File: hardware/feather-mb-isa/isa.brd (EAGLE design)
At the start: 91.4 x 95.2 mm, 16 parts, among them J1 EDGE-80PTH-RA, J2 M22PTH, J3 GREEN-3P-5.0, J4 GREEN-3P-5.0, J5 GREEN-3P-5.0, J6 GREEN-3P-5.0

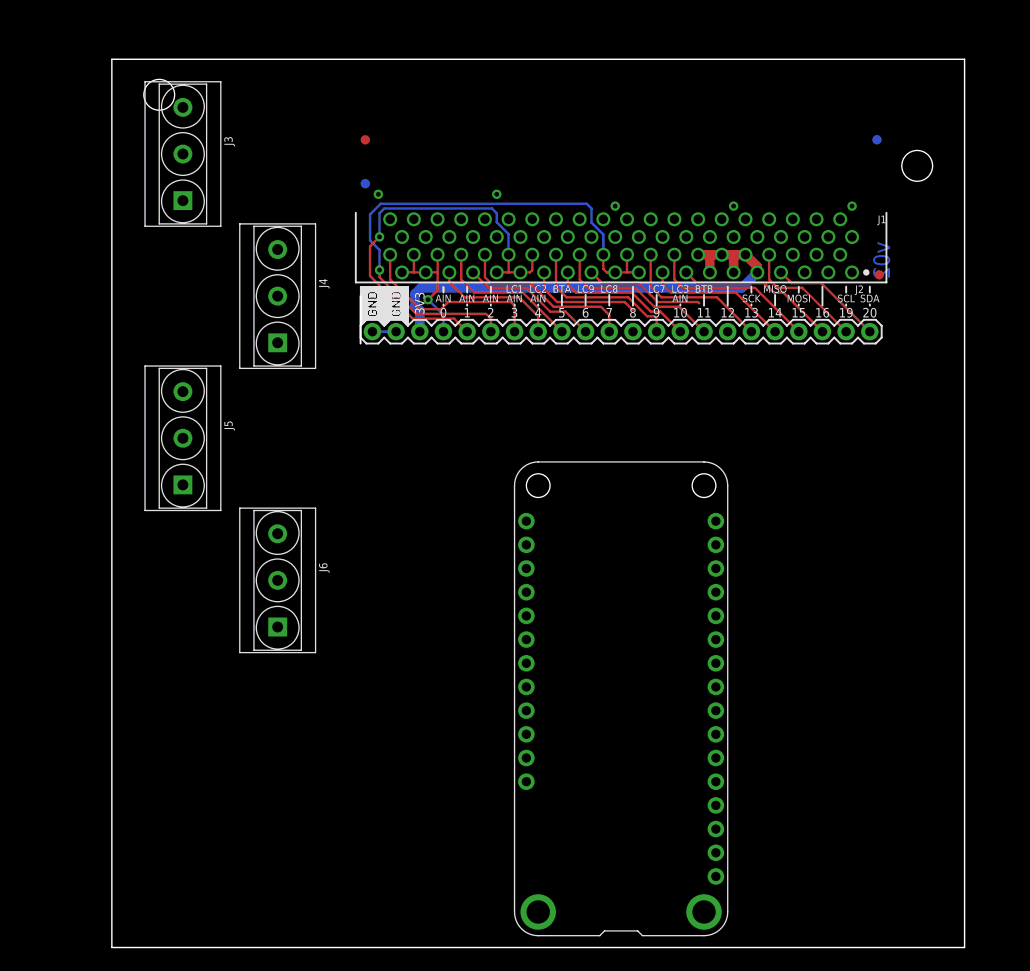
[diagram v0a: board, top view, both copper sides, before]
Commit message: Renamed midi.py
Now can be main.

Updated hardware. Looks ready for layout. Need to do some more
work in the middle. What to do with that space? Some neopixels?

Some buttons?

More headers?
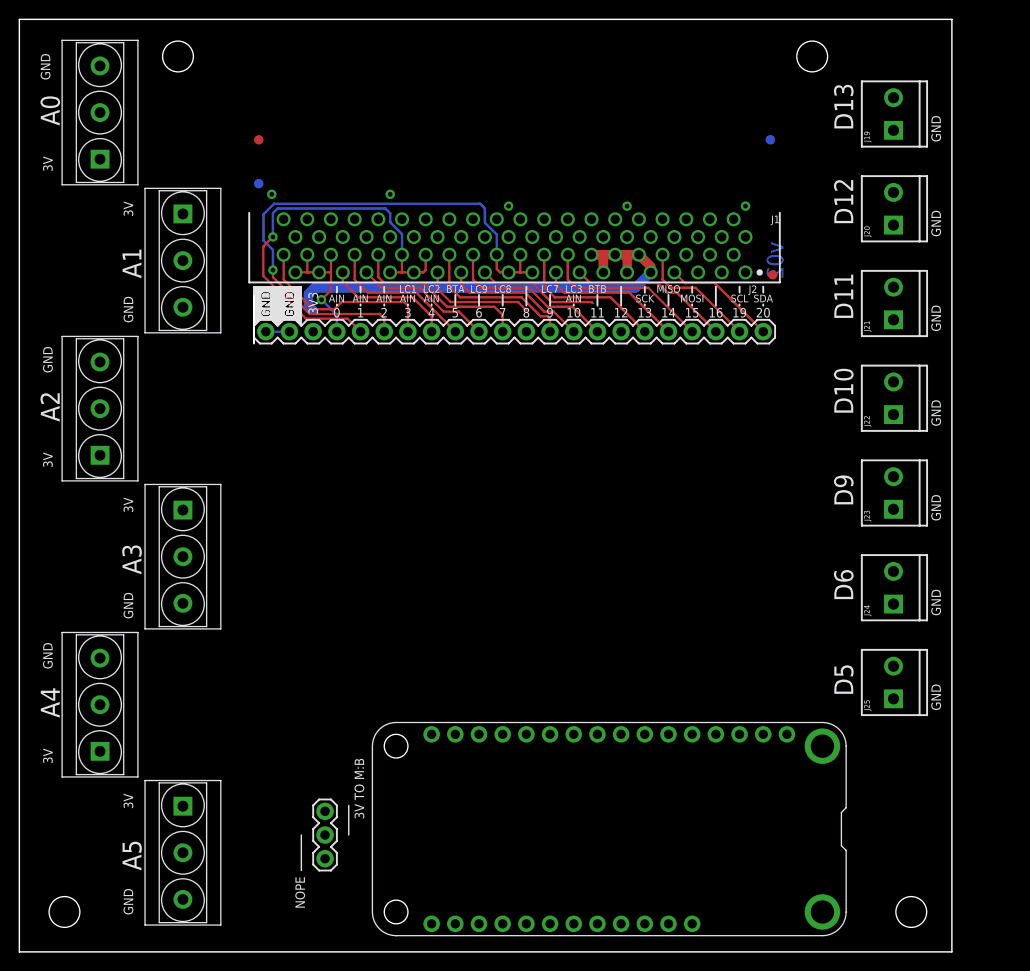
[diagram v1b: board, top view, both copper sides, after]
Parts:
- added H3, H4: STAND-OFF, SparkFun-Electromechanical:STAND-OFF
- added J12: (no value), SparkFun-Connectors:1X03
- added J19, J20, J21, J22, J23, J24, J25: (no value), SparkFun-Connectors:SCREWTERMINAL-3.5MM-2
- added J7, J8: GREEN-3P-5.0, Seeed-Connector:H3-5.0-15.5X8.0MM
- moved MS1 26.2 mm to (73.7, -25.4), turned to 180 degrees
- moved H2 16.3 mm to (70.0, 46.0)
- moved FD3 11.4 mm to (65.5, 37.1)
- moved U$2 11.4 mm to (15.2, 17.1)
- moved FD1 11.4 mm to (10.7, 37.1)
- moved FD4 11.4 mm to (10.7, 32.4)
- moved J1 11.4 mm to (38.1, 22.9)
- moved J2 11.4 mm to (11.4, 16.5)
- moved LOGO3 11.4 mm to (16.5, 34.3)
- moved U$1 11.4 mm to (10.2, 17.1)
- moved FD2 11.4 mm to (65.8, 22.6)
- moved J4 10.9 mm to (2.54, 24.1), turned to 0 degrees
- moved J6 10.5 mm to (2.54, -7.62), turned to 0 degrees
- moved J3 9.94 mm to (-6.35, 40.0)
- moved J5 9.44 mm to (-6.35, 8.26)
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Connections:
- removed net 19: J1.A8, J2.21
- removed net 20: J1.A7, J2.22
- removed net M0RX: J2.16
- removed net M0TX: J2.12
- new net 3V: J12.2, MS1.2
- new net D10: J22.2, MS1.22
- new net D11: J23.2, MS1.23
- new net D12: J24.2, MS1.24
- new net D13: J25.2, MS1.25
- new net D5: J19.2, MS1.19
- new net D6: J20.2, MS1.20
- new net D9: J21.2, MS1.21
- new net M4A0: J3.2, MS1.5
- new net M4A1: J4.2, MS1.6
- new net M4A2: J5.2, MS1.7
- new net M4A3: J6.2, MS1.8
- new net M4A4: J7.2, MS1.9
- new net M4A5: J8.2, MS1.10
- new net M4RX: J2.12, MS1.14
- new net M4TX: J2.16, MS1.15
- new net MB3V: J12.1, J2.3
- new net SCL: J1.A8, J2.21, MS1.18
- new net SDA: J1.A7, J2.22, MS1.17
- net 10: no longer J6.2
- net 2: no longer J3.2
- net 3: no longer J4.2
- net 3.3V: now also J7.1, J8.1; no longer J2.3
- net 4: no longer J5.2
- net GND: now also J19.1, J20.1, J21.1, J22.1, J23.1, J24.1, J25.1, J7.3, J8.3
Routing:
- net SCL: track 0.00 -> 13.2 mm
- net 19: track 13.2 -> 0.00 mm
- net 20: track 12.2 -> 0.00 mm
- net SDA: track 0.00 -> 12.2 mm
- net 3.3V: track 53.3 -> 51.0 mm
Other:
- board size 91.4 x 95.2 mm -> 100 x 100 mm
- board text added: "3V"
- board text added: "3V TO M:B"
- board text added: "A0"
- board text added: "A1"
- board text added: "A2"
- board text added: "A3"
- board text added: "A4"
- board text added: "A5"
- board text added: "D10"
- board text added: "D11"
- board text added: "D12"
- board text added: "D13"
- board text added: "D5"
- board text added: "D6"
- board text added: "D9"
- board text added: "GND"
- board text added: "NOPE"

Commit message: Changes.
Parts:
- added J10: (no value), SparkFun-Connectors:1X16_LOCK
- added J11: (no value), SparkFun-Connectors:SCREWTERMINAL-3.5MM-3
- added J9: (no value), SparkFun-Connectors:1X12_LOCK
- added MS2: FEATHERWING_NODIM, adafruit:FEATHERWING_DIM
- added U$3: LYNX#CORO#UNUM#PNG, lynx#coro#unum#png:LYNX#CORO#UNUM#PNG
- added U$4: LYNX#CORO#UNUM#PNG, big-lynx:LYNX#CORO#UNUM#PNG
- moved J12 75.6 mm to (0.64, 38.7), turned to 0 degrees
- moved LOGO3 55.7 mm to (57.1, -3.81), turned to 60.2 degrees
- moved MS1 13.7 mm to (61.0, -20.3)
- turned J4 to 180 degrees
- turned J6 to 180 degrees
- turned J8 to 180 degrees
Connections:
- removed net 3V: J12.2, MS1.2
- new net AREF: J10.3, MS1.3, MS2.3
- new net EN: J9.11, MS1.27, MS2.27
- new net N$15: J10.16, MS2.16
- new net QOWI: J10.12, MS1.12, MS2.12
- new net RESET: J10.1, MS1.1, MS2.1
- new net SCK: J10.11, MS1.11, MS2.11
- new net USB: J9.10, MS1.26, MS2.26
- new net VBAT: J9.12, MS1.28, MS2.28
- new net WOQI: J10.13, MS1.13, MS2.13
- net 3.3V: now also J10.2, J11.3, J12.2, MS1.2, MS2.2; no longer J1.A10, J1.A11, J1.A12, J1.A13, J1.A14, J1.A9
- net D10: now also J9.6, MS2.22
- net D11: now also J9.7, MS2.23
- net D12: now also J9.8, MS2.24
- net D13: now also J9.9, MS2.25
- net D5: now also J11.2, J9.3, MS2.19
- net D6: now also J9.4, MS2.20
- net D9: now also J9.5, MS2.21
- net GND: now also J10.4, J11.1, MS2.4
- net M4A0: now also J10.5, MS2.5
- net M4A1: now also J10.6, MS2.6
- net M4A2: now also J10.7, MS2.7
- net M4A3: now also J10.8, MS2.8
- net M4A4: now also J10.9, MS2.9
- net M4A5: now also J10.10, MS2.10
- net M4RX: now also J10.14, MS2.14
- net M4TX: now also J10.15, MS2.15
- net MB3V: now also J1.A10, J1.A11, J1.A12, J1.A13, J1.A14, J1.A9
- net SCL: now also J9.2, MS2.18
- net SDA: now also J9.1, MS2.17
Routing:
- net GND: track 2.54 -> 402.5 mm
- net 3.3V: track 51.0 -> 295.4 mm, vias 0 -> 2
- net D5: track 0.00 -> 126.1 mm
- net D6: track 0.00 -> 115.6 mm
- net SDA: track 12.2 -> 121.2 mm, vias 0 -> 2
- net SCL: track 13.2 -> 117.3 mm
- net M4A0: track 0.00 -> 103.0 mm
- net D9: track 0.00 -> 102.9 mm
- net D10: track 0.00 -> 97.0 mm
- net D11: track 0.00 -> 90.3 mm
- net MB3V: track 0.00 -> 88.4 mm
- net D13: track 0.00 -> 84.6 mm
- net M4A1: track 0.00 -> 82.4 mm
- net D12: track 0.00 -> 81.5 mm
- net M4TX: track 0.00 -> 78.2 mm
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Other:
- board text added: "Open Hardware Designed By Matt Jadud 2019 Based on work by adafruit.com & sparkfun.com"
- board text removed: "v02"

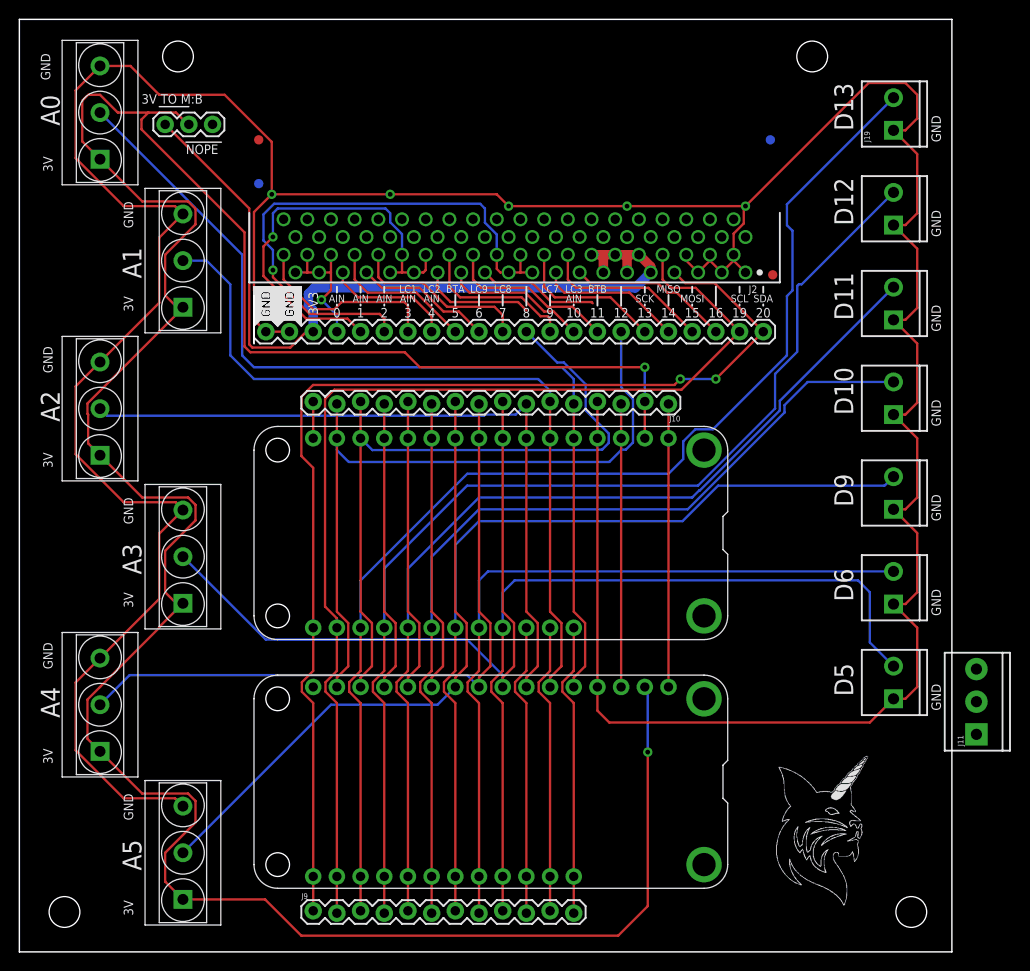
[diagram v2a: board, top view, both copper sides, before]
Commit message: Updates to the board.
It would be good to have one pin with power. The ids are all out of order on the RH side.
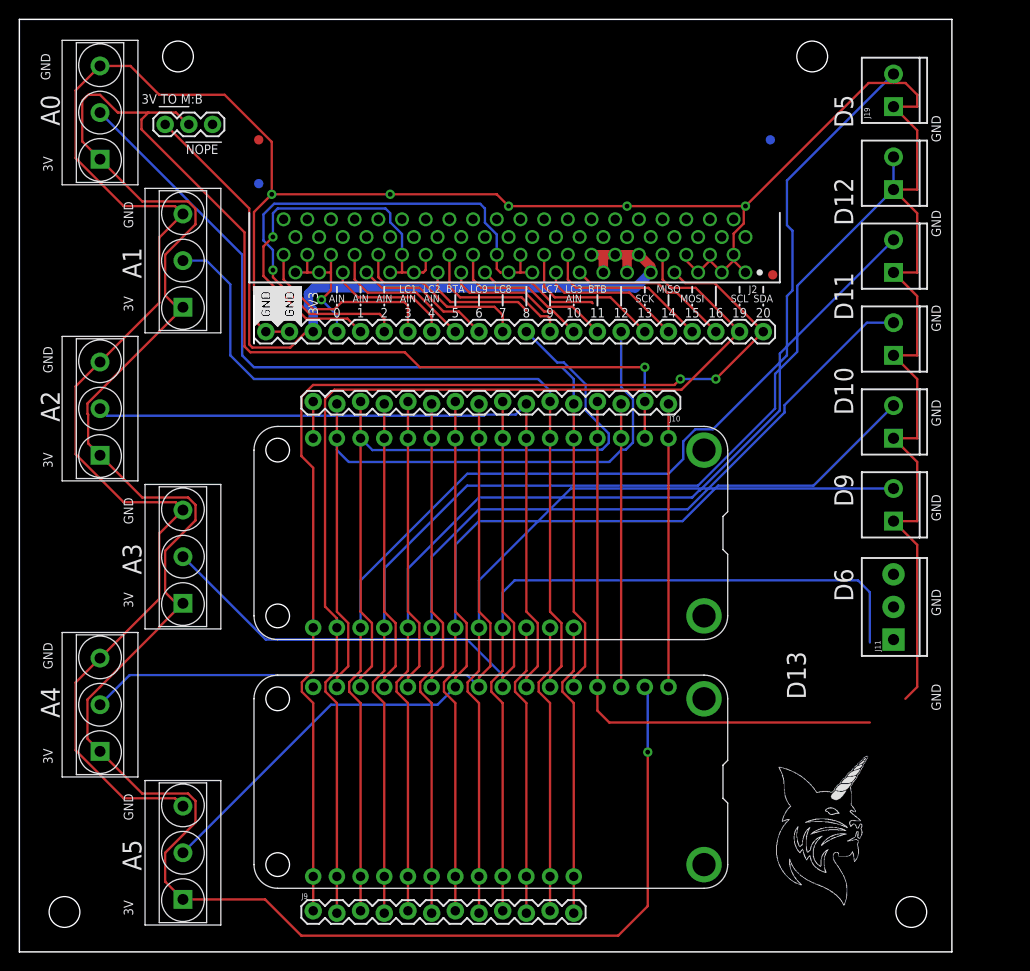
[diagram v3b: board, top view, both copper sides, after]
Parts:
- removed J25: (no value), SparkFun-Connectors:SCREWTERMINAL-3.5MM-2
- moved J11 13.5 mm to (78.7, -16.5)
- moved J24 8.89 mm to (78.7, -3.81)
- moved J23 7.62 mm to (78.7, 5.08)
- moved J22 6.35 mm to (78.7, 14.0)
- moved J21 5.08 mm to (78.7, 22.9)
- moved J20 3.81 mm to (78.7, 31.8)
- moved J19 2.54 mm to (78.7, 40.6)
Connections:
- net D13: no longer J25.2
- net GND: no longer J25.1
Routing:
- net D9: track 102.9 -> 108.0 mm
- net D12: track 81.5 -> 85.2 mm
- net D6: track 115.6 -> 119.2 mm
- net D13: track 84.6 -> 81.0 mm
- net D11: track 90.3 -> 93.4 mm
- net D10: track 97.0 -> 99.6 mm
- net D5: track 126.1 -> 128.7 mm

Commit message: Moving things around.
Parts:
- J3, J4, J5, J6, J7, J8: value GREEN-3P-5.0 -> (none); device Seeed-Connector:H3-5.0-15.5X8.0MM -> SparkFun-Connectors:SCREWTERMINAL-3.5MM-3
- moved J8 22.2 mm to (-6.35, -19.1), turned to 270 degrees
- moved J7 17.1 mm to (-6.35, -6.35), turned to 270 degrees
- moved J6 16.6 mm to (-6.35, 6.35), turned to 270 degrees
- moved J4 11.7 mm to (-6.35, 31.8), turned to 270 degrees
- moved J5 10.8 mm to (-6.35, 19.1), turned to 270 degrees
- moved J12 7.41 mm to (4.45, 32.4), turned to 90 degrees
- moved U$3 7.41 mm to (77.5, -33.0)
- moved J11 5.08 mm to (78.7, -21.6)
- moved J3 4.45 mm to (-6.35, 44.5), turned to 270 degrees
- moved J24 3.81 mm to (78.7, -7.62)
- moved J23 2.54 mm to (78.7, 2.54)
- moved J19 2.54 mm to (78.7, 43.2)
- moved J20 1.27 mm to (78.7, 33.0)
- moved J22 1.27 mm to (78.7, 12.7)
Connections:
- removed net 12: J1.A23
- removed net 8: J1.A27
- net D13: now also J11.2
- net D5: no longer J11.2
- net M4A3: now also J8.2; no longer J6.2
- net M4A4: now also J6.2; no longer J7.2
- net M4A5: now also J7.2; no longer J8.2
- net M4RX: now also J1.A27
- net M4TX: now also J1.A23
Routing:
- net GND: track 402.1 -> 328.3 mm, vias 5 -> 0
- net 3.3V: track 295.4 -> 227.2 mm, vias 2 -> 0
- net M4TX: track 78.2 -> 95.4 mm
- net M4RX: track 75.1 -> 89.6 mm
- net M4A1: track 82.4 -> 96.4 mm
- net MB3V: track 88.4 -> 74.4 mm
- net 12: track 12.9 -> 0.00 mm
- net 8: track 12.2 -> 0.00 mm
- net D13: track 81.0 -> 87.6 mm
- net M4A5: track 68.2 -> 74.6 mm
- net M4A3: track 72.4 -> 78.8 mm
- net M4A0: track 103.0 -> 107.6 mm
- net M4A2: track 77.9 -> 81.8 mm
- net D5: track 128.7 -> 131.2 mm
- net D6: track 119.2 -> 120.9 mm
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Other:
- board text added: "FEATHER ONE"
- board text added: "FEATHER TWO"
- board text added: "MICRO:BIT GOES HERE LEDS FACING UP"
- board text added: "https://lynxruf.us/corounum"

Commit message: About to change Python... `:
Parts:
- moved U$3 76.2 mm to (1.27, -35.6)
- moved J4 3.18 mm to (-8.89, 33.7)
- moved J6 3.18 mm to (-8.89, 8.26)
- moved J8 3.18 mm to (-8.89, -17.1)
- moved J7 3.17 mm to (-8.89, -4.45)
- moved J5 3.17 mm to (-8.89, 21.0)
- moved J3 3.17 mm to (-8.89, 46.4)
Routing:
- net GND: track 328.3 -> 332.7 mm
- net M4A3: track 78.8 -> 82.1 mm
- net M4A5: track 74.6 -> 77.9 mm
- net M4A2: track 81.8 -> 85.2 mm
- net M4A1: track 96.4 -> 99.7 mm
- net 3.3V: track 227.2 -> 230.5 mm
- net M4A0: track 107.6 -> 110.5 mm
- net M4A4: track 74.0 -> 75.7 mm
